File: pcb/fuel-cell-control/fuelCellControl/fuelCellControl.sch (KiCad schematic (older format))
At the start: 36 parts, among them J1 Conn_01x15_Male, J2 Conn_01x02_Male, J3 Conn_01x15_Male, J4 Conn_01x02_Male, J5 Conn_01x02_Male, J6 Conn_01x16_Male, J7 Conn_01x16_Male, Q1 Q_NMOS_GDS, Q2 Q_NMOS_GDS, Q3 Q_NMOS_GDS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

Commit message: initial pcb design
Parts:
- removed J5: Conn_01x02_Male, symbol Connector:Conn_01x02_Male
- removed J6, J7: Conn_01x16_Male, symbol Connector:Conn_01x16_Male
- removed Q1: Q_NMOS_GDS, Package_TO_SOT_SMD:SOT-323_SC-70, symbol Device:Q_NMOS_GSD
- removed TP3, TP4, TP9: TestPoint, symbol Connector:TestPoint
- added H1, H2, H3, H4: MountingHole, MountingHole:MountingHole_2.2mm_M2, symbol Mechanical:MountingHole
- added J3: LittlePump, Connector_Molex:Molex_Mini-Fit_Jr_5569-02A2_2x01_P4.20mm_Horizontal, symbol Connector:Conn_01x02_Male
- added J6: Relay, Connector_Molex:Molex_Mini-Fit_Jr_5569-02A2_2x01_P4.20mm_Horizontal, symbol Connector:Conn_01x02_Male
- added J7, J8: Conn_01x10_Male, Connector_Phoenix_MC:PhoenixContact_MCV_1,5_10-G-3.5_1x10_P3.50mm_Vertical, symbol Connector:Conn_01x10_Male
- added Q2: Q_NMOS_GDS, Package_TO_SOT_SMD:SOT-323_SC-70, symbol Device:Q_NMOS_GSD
- added TP2, TP6: TestPoint, Connector_PinSocket_2.54mm:PinSocket_1x01_P2.54mm_Vertical, symbol Connector:TestPoint
- A1: DigikeyPN (none) -> 1050-ABX00028-ND
- C1: footprint (none) -> Capacitor_SMD:C_1206_3216Metric; DigikeyPN (none) -> 478-8875-1-ND
- C2, C3: footprint (none) -> Capacitor_SMD:C_0805_2012Metric; DigikeyPN (none) -> 478-3286-1-ND
- D1, D2, D3: footprint (none) -> LED_SMD:LED_0201_0603Metric
- F1: value 3586KTR -> Fuse; footprint (none) -> digikey-footprints:3586KTR
- J1: renamed from J2; footprint (none) -> Connector_Molex:Molex_Mini-Fit_Jr_5569-02A2_2x01_P4.20mm_Horizontal
- J2: renamed from J1; footprint (none) -> Connector_PinSocket_2.54mm:PinSocket_1x15_P2.54mm_Vertical; DigikeyPN (none) -> S7013-ND
- J4: value Conn_01x02_Male -> BigPump; footprint (none) -> Connector_Molex:Molex_Mini-Fit_Jr_5569-02A2_2x01_P4.20mm_Horizontal
- J5: renamed from J3; footprint (none) -> Connector_PinSocket_2.54mm:PinSocket_1x15_P2.54mm_Vertical; DigikeyPN (none) -> S7013-ND
- TP1: renamed from TP2; footprint (none) -> Connector_PinSocket_2.54mm:PinSocket_1x01_P2.54mm_Vertical
- TP3: renamed from TP1; footprint (none) -> Connector_PinSocket_2.54mm:PinSocket_1x01_P2.54mm_Vertical
- TP4: renamed from TP5; footprint (none) -> Connector_PinSocket_2.54mm:PinSocket_1x01_P2.54mm_Vertical
- TP5: renamed from TP6; footprint (none) -> Connector_PinSocket_2.54mm:PinSocket_1x01_P2.54mm_Vertical
- TP7, TP8: footprint (none) -> Connector_PinSocket_2.54mm:PinSocket_1x01_P2.54mm_Vertical
- U3, U4: footprint (none) -> digikey-footprints:SOIC-28_W7.5mm
- renumbered Q2 to Q1
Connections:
- net EveryPin19 is gone; now on net MuxAnalog: A1.19 (A0), J5.4 (Pin_4)
- net +5V: no longer C1.1, C3.1, F1.1, J4.1 (Pin_1), TP3.1, U1.3 (VI), U3.1 (VDD), U4.1 (VDD)
- net GND: now also Q2.2 (S)
- net at J4.2 (Pin_2): now also Q2.3 (D), TP2.1
- net at Q1.3 (D), TP1.1: now also J3.2 (Pin_2)
- net MuxAnalog: now reaches R4.2, R5.1
- net at U3.10 (S10): now also J7.10 (Pin_10)
- net at U3.11 (S9): now also J7.9 (Pin_9)
- net at U2.4: now also TP8.1, U4.18 (EN); no longer U3.18 (EN)
- net at U3.19 (S1): now also J7.1 (Pin_1)
- net at U3.20 (S2): now also J7.2 (Pin_2)
- net at U3.21 (S3): now also J7.3 (Pin_3)
- net at U3.22 (S4): now also J7.4 (Pin_4)
- net at U3.23 (S5): now also J7.5 (Pin_5)
- net at U3.24 (S6): now also J7.6 (Pin_6)
- net at U3.25 (S7): now also J7.7 (Pin_7)
- net at U3.26 (S8): now also J7.8 (Pin_8)
- net at U3.4 (S16): now also J8.6 (Pin_6)
- net at U3.5 (S15): now also J8.5 (Pin_5)
- net at U3.6 (S14): now also J8.4 (Pin_4)
- net at U3.7 (S13): now also J8.3 (Pin_3)
- net at U3.8 (S12): now also J8.2 (Pin_2)
- net at U3.9 (S11): now also J8.1 (Pin_1)
- net at U4.19 (S1): now also J8.7 (Pin_7)
- net at U4.20 (S2): now also J8.8 (Pin_8)
- net at U4.21 (S3): now also J8.9 (Pin_9)
- net at U4.22 (S4): now also J8.10 (Pin_10)
- net at Q3.3 (D): now also J6.2 (Pin_2), TP6.1
- net Big_Pump renamed BigPump
- net BigPump: now also Q2.1 (G)
- net Enable_Pin renamed EnablePin
- net EnablePin: now also U3.18 (EN); no longer TP8.1, U4.18 (EN)
- net EveryPin1 renamed TX1
- net EveryPin10 renamed MuxSelect3
- net EveryPin11 renamed Relay
- net EveryPin13 renamed LittlePump
- net EveryPin14 renamed MOSI
- net EveryPin15 renamed MISO
- net EveryPin16 renamed SCK
- net EveryPin17 renamed Nano3V3Out
- net EveryPin18 renamed AREF
- net EveryPin2 renamed RX1
- net EveryPin20 renamed Analog1
- net EveryPin21 renamed Analog2
- net EveryPin22 renamed Analog3
- net EveryPin23 renamed Analog4_SDA
- net EveryPin24 renamed Analog5_SCL
- net EveryPin25 renamed Analog6
- net EveryPin26 renamed Analog7
- net EveryPin27 renamed Nano5VOut
- net EveryPin28 renamed RESET2
- net EveryPin3 renamed RESET1
- net EveryPin6 renamed D3_PWM
- net EveryPin7 renamed MuxSelect0
- net EveryPin8 renamed MuxSelect1
- net EveryPin9 renamed MuxSelect2
- new net +12V: C1.1, C3.1, F1.1, J3.1 (Pin_1), J4.1 (Pin_1), J6.1 (Pin_1), TP3.1, U1.3 (VI), U3.1 (VDD), U4.1 (VDD)
- no-connect marks 0 -> 12
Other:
- moved on the sheet: C1, C2, C3, D1, F1, J1, Q1, R1, R4, R5, TP1, TP3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

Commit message: updated based on design review
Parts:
- removed U2: 74AHCT1G04, Package_TO_SOT_SMD:SOT-353_SC-70-5, symbol 74xGxx:74AHCT1G04
- added C4: 0.1uF, Capacitor_SMD:C_0603_1608Metric, symbol Device:C
- added R6: 820k, Resistor_SMD:R_0603_1608Metric, symbol Device:R
- added R7: 430k, Resistor_SMD:R_0603_1608Metric, symbol Device:R
- C1: value 10uF -> 1uF; footprint Capacitor_SMD:C_1206_3216Metric -> Capacitor_SMD:C_0603_1608Metric; DigikeyPN 478-8875-1-ND -> 490-12330-1-ND
- C2: value 0.1uF -> 1uF; footprint Capacitor_SMD:C_0805_2012Metric -> Capacitor_SMD:C_0603_1608Metric; symbol Device:CP -> Device:C; DigikeyPN 478-3286-1-ND -> 490-12330-1-ND
- C3: footprint Capacitor_SMD:C_0805_2012Metric -> Capacitor_SMD:C_0603_1608Metric; symbol Device:CP -> Device:C; DK_Details_Page (none) -> https://www.digikey.ca/en/products/detail/yageo/CC0603ZRY5V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; DigikeyPN 478-3286-1-ND -> 311-1343-1-ND
- D1, D2, D3: footprint LED_SMD:LED_0201_0603Metric -> LED_SMD:LED_0603_1608Metric; DigikeyPN 1497-1295-1-ND -> SML-D12W8WT86ACT-ND
- H1, H2, H3, H4: footprint MountingHole:MountingHole_2.2mm_M2 -> MountingHole:MountingHole_3.2mm_M3
- J1: value Conn_01x02_Male -> InputPower
- Q1, Q2, Q3: footprint Package_TO_SOT_SMD:SOT-323_SC-70 -> Package_TO_SOT_SMD:SOT-89-3
- R1, R2, R3: value 400ohms -> 1.5k; footprint Resistor_SMD:R_1206_3216Metric -> Resistor_SMD:R_0603_1608Metric; DK_Details_Page (none) -> https://www.digikey.ca/en/products/detail/te-connectivity-p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; DigikeyPN 13-RT1206BRD07400RLCT-ND -> A121524CT-ND
- R4: value 680k -> 820k; footprint Resistor_SMD:R_0402_1005Metric -> Resistor_SMD:R_0603_1608Metric; DigikeyPN A129661CT-ND -> 311-820KHRCT-ND
- R5: value 470k -> 430k; footprint Resistor_SMD:R_0402_1005Metric -> Resistor_SMD:R_0603_1608Metric; DigikeyPN A129842CT-ND -> CR0603-JW-434ELFCT-ND
- TP1: value TestPoint -> LPump
- TP2: value TestPoint -> BPump
- TP3: value TestPoint -> 12V
- TP4: value TestPoint -> GND
- TP5: value TestPoint -> 5V
- TP6: value TestPoint -> RelayT
- TP7: value TestPoint -> Mux1
- TP8: value TestPoint -> Mux2
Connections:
- net Nano5VOut is gone; now on net +5V: A1.27 (+5V), J5.12 (Pin_12)
- net +12V: now also U3.18 (EN), U4.18 (EN), C4.1
- net +5V: no longer A1.30 (VIN), J5.15 (Pin_15)
- net Analog1: now also R6.2, R7.1
- net GND: now also C4.2, R7.2
- net at R4.1, TP7.1, U3.28 (D): no longer U4.28 (D)
- net at TP8.1: now also U4.28 (D), R6.1; no longer U4.18 (EN)
- net EnablePin renamed D2
- net D2: no longer U3.18 (EN)
- new net VinNano: A1.30 (VIN), J5.15 (Pin_15)

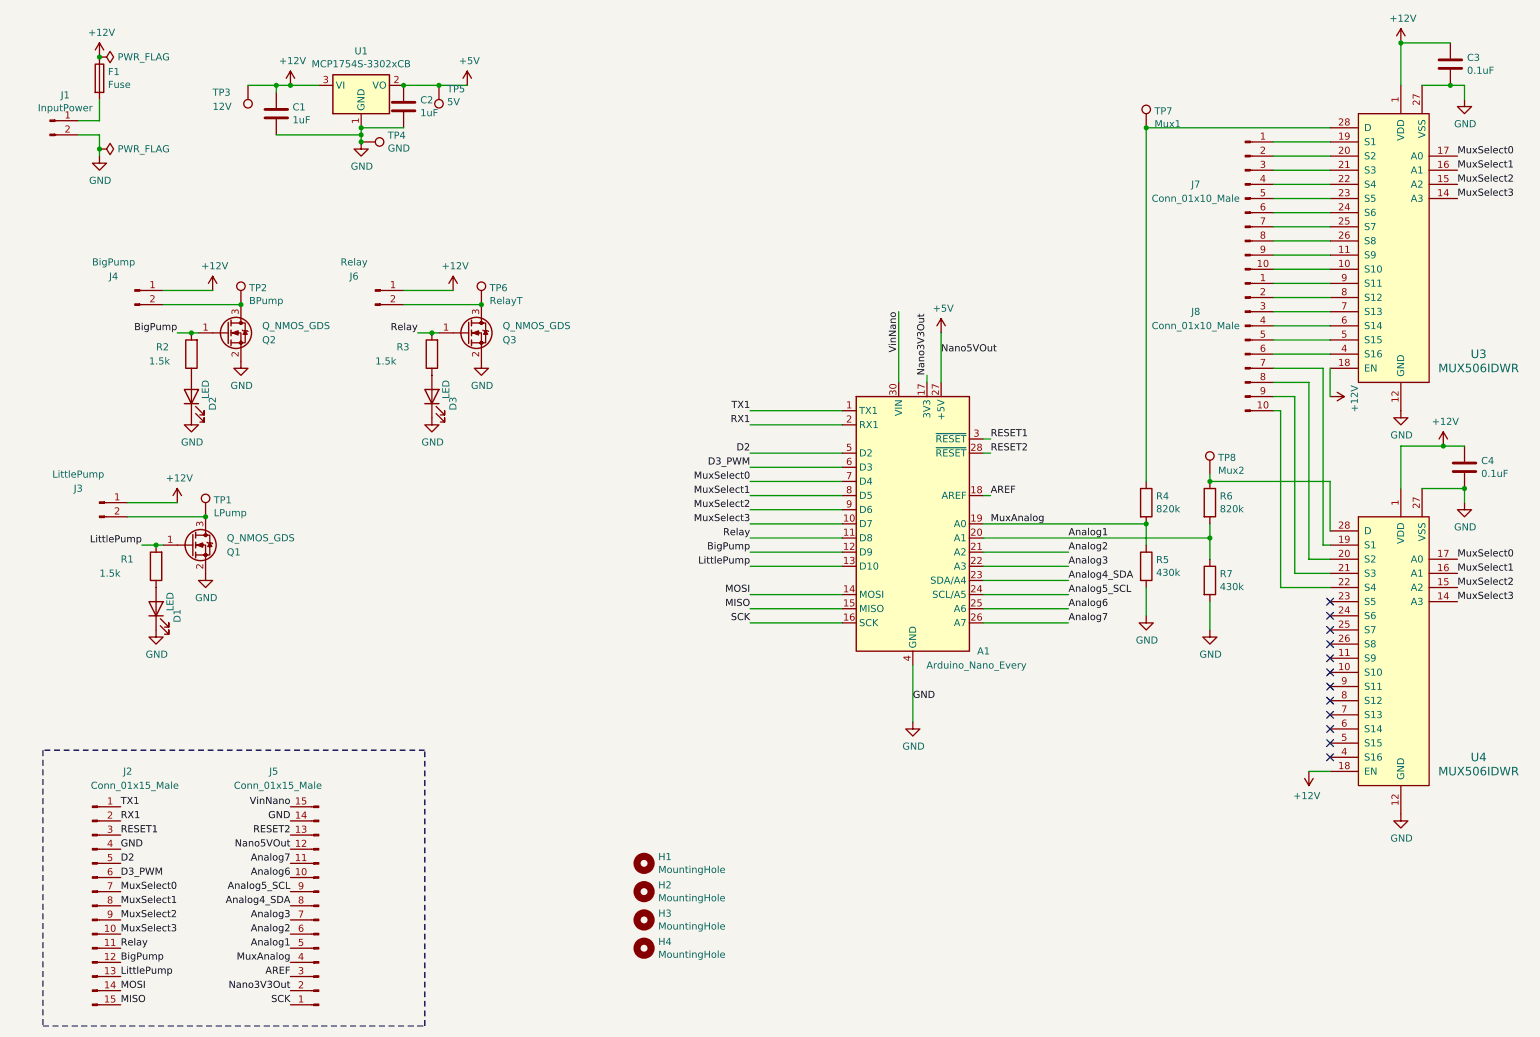
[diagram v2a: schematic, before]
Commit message: remove voltage regulator and update connector spacing and tracing
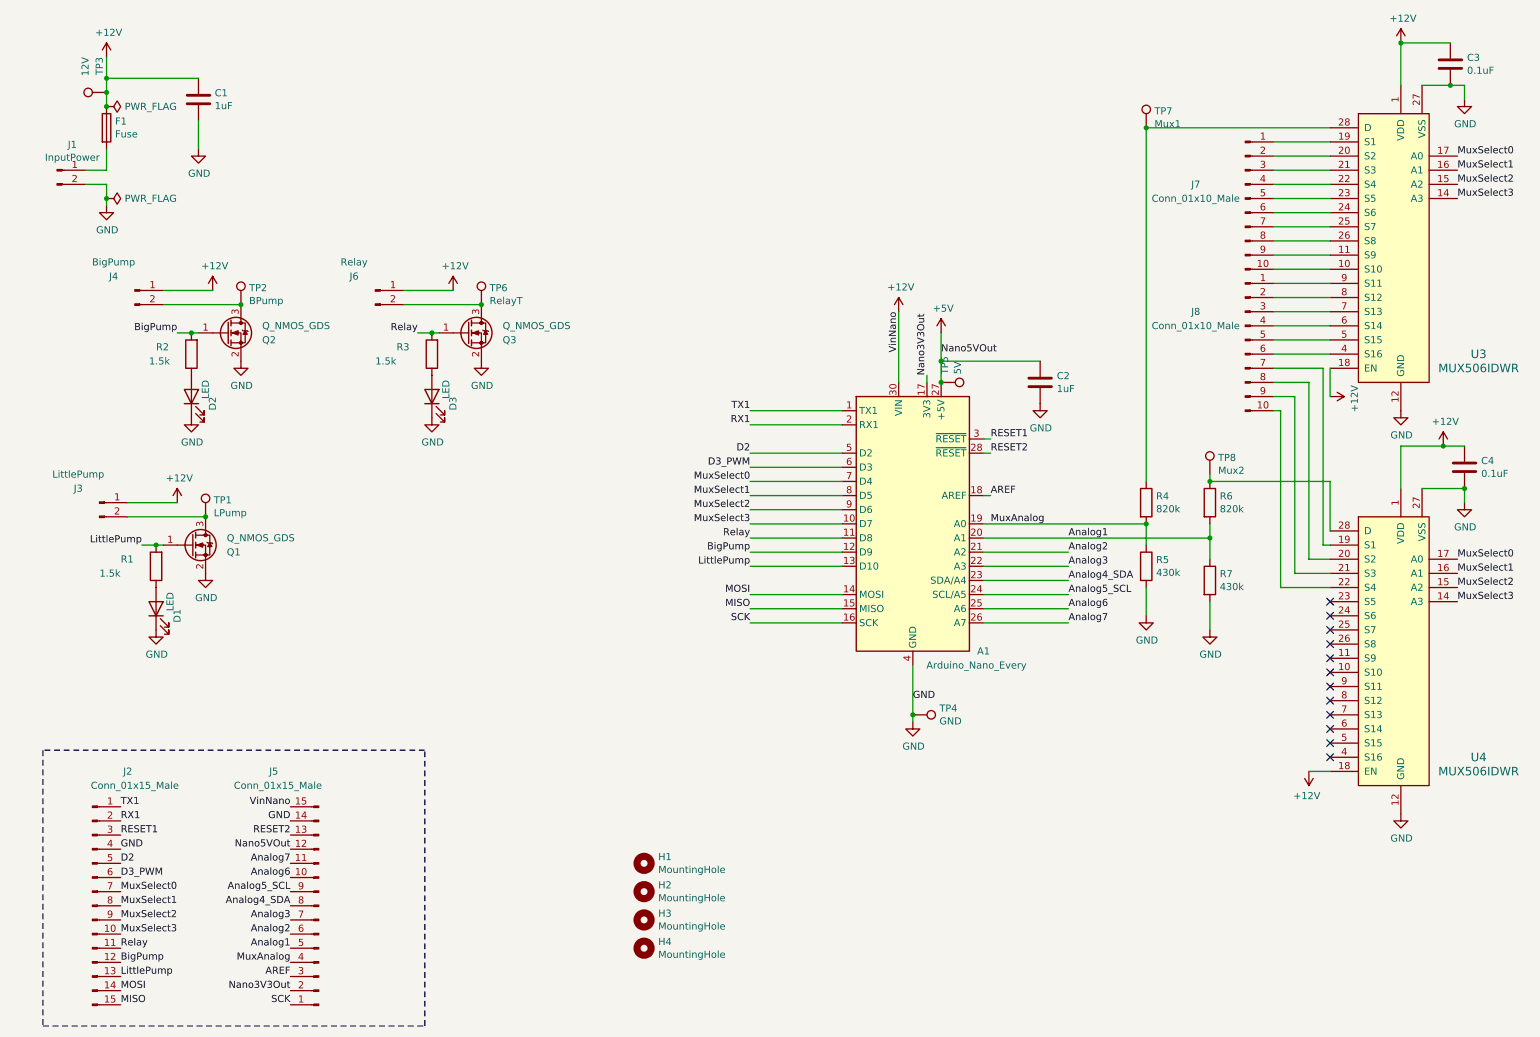
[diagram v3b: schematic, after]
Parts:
- removed U1: MCP1754S-3302xCB, Package_TO_SOT_SMD:SOT-23, symbol Regulator_Linear:MCP1754S-3302xCB
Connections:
- net VinNano is gone; now on net +12V: A1.30 (VIN), J5.15 (Pin_15)
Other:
- moved on the sheet: C1, C2, F1, J1, TP3, TP4, TP5
